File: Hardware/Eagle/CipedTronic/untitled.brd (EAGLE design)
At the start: 100 x 80 mm, 14 parts, among them IC1 ATMEGA48/88/168-PU, T1 BC547

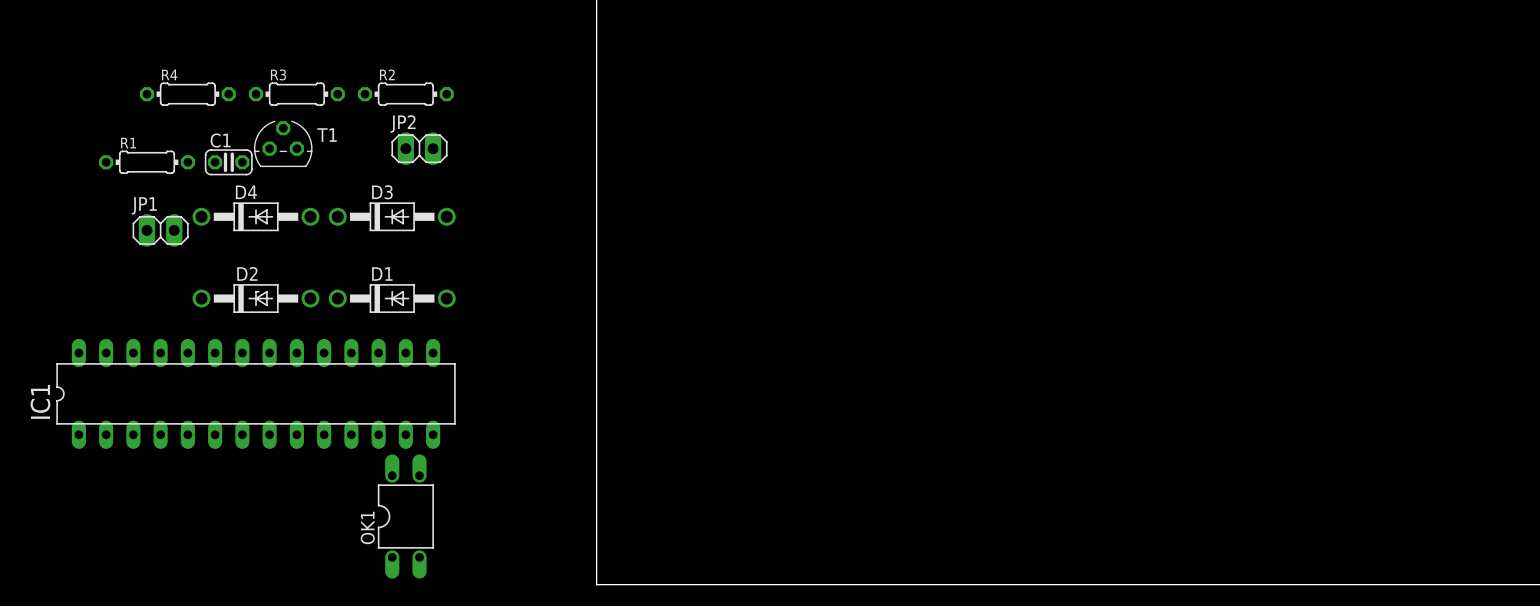
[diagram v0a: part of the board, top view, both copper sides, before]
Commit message: migration to seed xaio esp32
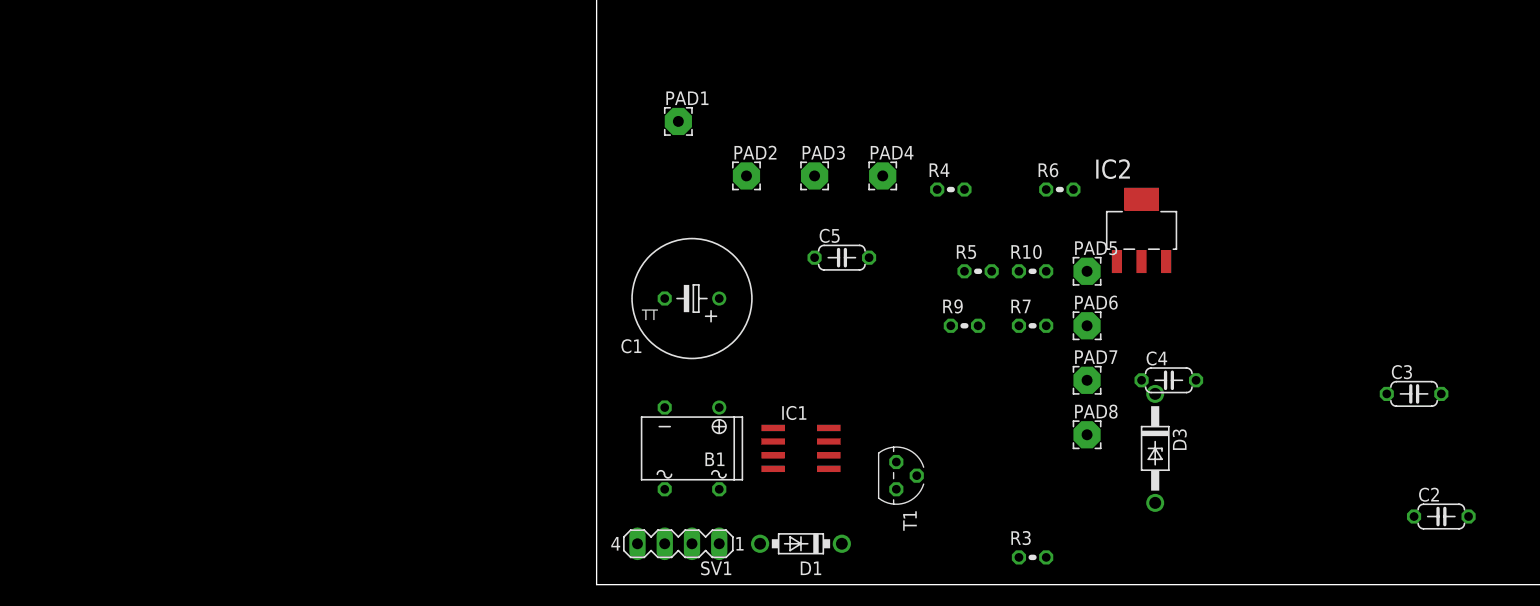
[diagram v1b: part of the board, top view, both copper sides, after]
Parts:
- removed D2: 1N4728, diode:DO41Z10
- removed D4: 1N4004, diode:DO41-10
- removed JP1, JP2: (no value), pinhead:1X02
- removed OK1: SFH610, optocoupler:DIL04
- removed R1, R2: (no value), rcl:0204/7
- added B1: (no value), rectifier:B-DIL
- added C2, C3, C4, C5: (no value), rcl:C050-024X044
- added IC2: LM1117MP-5.0, lm1117_11:SOT223
- added PAD1, PAD2, PAD3, PAD4, PAD5, PAD6, PAD7, PAD8: WIREPAD2,54/1,0, wirepad:2,54/1,0
- added R10, R5, R6, R7, R9: (no value), rcl:0204V
- added SV1: (no value), con-lstb:MA04-1
- C1: device rcl:C025-024X044 -> rcl:TT5D11
- D1: value 1N4004 -> 1N5818-T; device diode:DO41-10 -> diode:DO41-7.6
- D3: value 1N4004 -> 1N4728; device diode:DO41-10 -> diode:DO41Z10
- IC1: value ATMEGA48/88/168-PU -> LM358D; device atmega8:DIL28-3 -> linear:SO08
- R3, R4: device rcl:0204/7 -> rcl:0204V
- T1: value BC547 -> BC337
- moved R3 81.0 mm to (40.6, 2.54)
- moved D3 74.3 mm to (52.1, 12.7), turned to 270 degrees
- moved R4 71.7 mm to (33.0, 36.8)
- moved T1 64.8 mm to (27.9, 10.2), turned to 270 degrees
- moved IC1 51.1 mm to (19.1, 12.7), turned to 270 degrees
- moved C1 45.0 mm to (8.89, 26.7), turned to 180 degrees
- moved D1 44.4 mm to (19.1, 3.81), turned to 180 degrees
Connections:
- removed net N$6: IC1.2, JP1.1
- removed net N$7: OK1.2, T1.3
- new net +3V3: B1.+, C1.+, C4.1, IC1.8, PAD7.1, R3.2, R5.2, R7.2
- new net N$11: IC1.6, R5.1, R6.2
- new net N$12: PAD2.1, PAD3.1
- new net N$4: R9.2, T1.2
- new net V+: IC1.5, PAD1.1, T1.3
- net +5V: now also IC2.2, IC2.4, PAD6.1; no longer C1.1, IC1.20, IC1.7, OK1.3
- net GND: now also B1.-, C1.-, C4.2, C5.1, IC1.2, IC1.4, IC2.1, PAD4.1, PAD8.1, R10.1, R6.1; no longer C1.2, D2.A, D4.C, IC1.22, IC1.8, JP2.1, R3.2, R4.2
- net N$1: now also B1.AC1, C5.2, R4.1, SV1.3, SV1.4; no longer D1.C, R1.2
- net N$10: now also D3.A, R10.2; no longer IC1.3, JP1.2
- net N$2: now also B1.AC2, SV1.1, SV1.2; no longer R3.1, T1.1
- net N$3: now also IC1.1, PAD5.1, R3.1; no longer D3.A, R2.2, T1.2
- net N$5: now also D1.A, D1.C, IC1.3, R4.2; no longer D2.C, OK1.1, R1.1, R2.1
- net N$8: now also IC1.7, R7.1, R9.1; no longer D1.A, JP2.2
- net N$9: now also D3.C, IC2.3, T1.1; no longer IC1.11, OK1.4, R4.1

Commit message: Cipedtronic with esp32
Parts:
- added D2: 1N4728, diode:DO41Z10
- added D4, D5: 1N5818-T, diode:DO41-7.6
- added R1, R8: 10k, rcl:0204V
- added R2: 1m, rcl:0204V
- C2: value (none) -> 0,1uf
- C3: value (none) -> 0.33uf
- R3: value (none) -> 10k
- moved R3 57.7 mm to (3.81, -41.9)
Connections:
- net N$2 renamed V-
- new net N$6: IC1.3, R1.1, R2.2
- new net N$7: D4.A, D4.C, D5.A, IC1.2, R3.2
- net +3V3: now also R3.1, R8.1; no longer R3.2
- net +5V: now also C2.1
- net GND: now also C2.2, C3.2, D2.A, D5.C; no longer IC1.2
- net N$3: now also R2.1, R8.2; no longer R3.1
- net N$5: now also D2.C, R1.2; no longer IC1.3
- net N$9: now also C3.1

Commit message: Rename sketch Extend Timer Add namespace
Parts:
- removed C1: (no value), rcl:TT5D11
- removed D3: 1N4728, diode:DO41Z10
- removed R10, R9: (no value), rcl:0204V
- removed T1: BC337, transistor:TO92
- added PAD10, PAD9: Light on/off switch, wirepad:2,15/1,0
- added Q1, Q3: FDD4141TO252, transistor-fet:TO252
- PAD1: value WIREPAD2,54/1,0 -> Light on/off ESP32; device wirepad:2,54/1,0 -> wirepad:2,15/1,0
- PAD2: value WIREPAD2,54/1,0 -> 5V ESP32; device wirepad:2,54/1,0 -> wirepad:2,15/1,0
- PAD3: value WIREPAD2,54/1,0 -> 3.3V ESP32; device wirepad:2,54/1,0 -> wirepad:2,15/1,0
- PAD4, PAD5: value WIREPAD2,54/1,0 -> LED; device wirepad:2,54/1,0 -> wirepad:2,15/1,0
- PAD6: value WIREPAD2,54/1,0 -> Pulses ESP32; device wirepad:2,54/1,0 -> wirepad:2,15/1,0
- PAD7, PAD8: value WIREPAD2,54/1,0 -> Super Cap; device wirepad:2,54/1,0 -> wirepad:2,15/1,0
- R5: value (none) -> 10k; device rcl:0204V -> rcl:MINI_MELF-0204W
- R6, R7: value (none) -> 10k
- moved R8 72.4 mm to (6.35, 24.1)
- moved R2 69.3 mm to (36.8, 40.6)
- moved D4 65.9 mm to (22.9, 36.8)
- moved D5 64.3 mm to (15.2, 29.2)
- moved R3 63.1 mm to (14.0, 20.3)
- moved R1 51.6 mm to (12.7, 35.6)
- moved C3 49.5 mm to (26.7, 19.1)
- moved PAD6 44.9 mm to (1.27, 17.8)
- moved PAD7 44.9 mm to (1.27, 12.7)
- moved PAD8 44.9 mm to (1.27, 7.62)
- moved R7 44.3 mm to (1.27, 44.5)
- moved C2 37.5 mm to (45.7, 24.1), turned to 90 degrees
- moved D2 36.1 mm to (17.8, 25.4)
- moved C4 26.9 mm to (26.7, 15.2)
- moved PAD3 21.6 mm to (1.27, 27.9)
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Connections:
- removed net N$10: D3.A, R10.2
- removed net N$11: IC1.6, R5.1, R6.2
- removed net N$12: PAD2.1, PAD3.1
- new net N$13: D1.A, R4.2
- new net N$2: PAD4.1, Q3.3
- net +3V3: now also PAD10.1, PAD2.1; no longer C1.+, R5.2, R7.2
- net +5V: now also PAD3.1; no longer PAD6.1
- net GND: now also PAD5.1, R5.2, R7.2; no longer C1.-, PAD4.1, R10.1, R6.1
- net N$3: now also PAD6.1; no longer PAD5.1
- net N$4: now also C3.1, IC2.3, Q1.3; no longer R9.2, T1.2
- net N$5: no longer D1.A, R4.2
- net N$8: now also PAD1.1, PAD9.1, Q3.1; no longer IC1.7, R9.1
- net N$9: now also Q1.1, R5.1, R6.2; no longer C3.1, D3.C, IC2.3, T1.1
- net V+: now also Q1.2, Q3.2, R6.1; no longer IC1.5, PAD1.1, T1.3
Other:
- board size 100 x 80 mm -> 50 x 50 mm

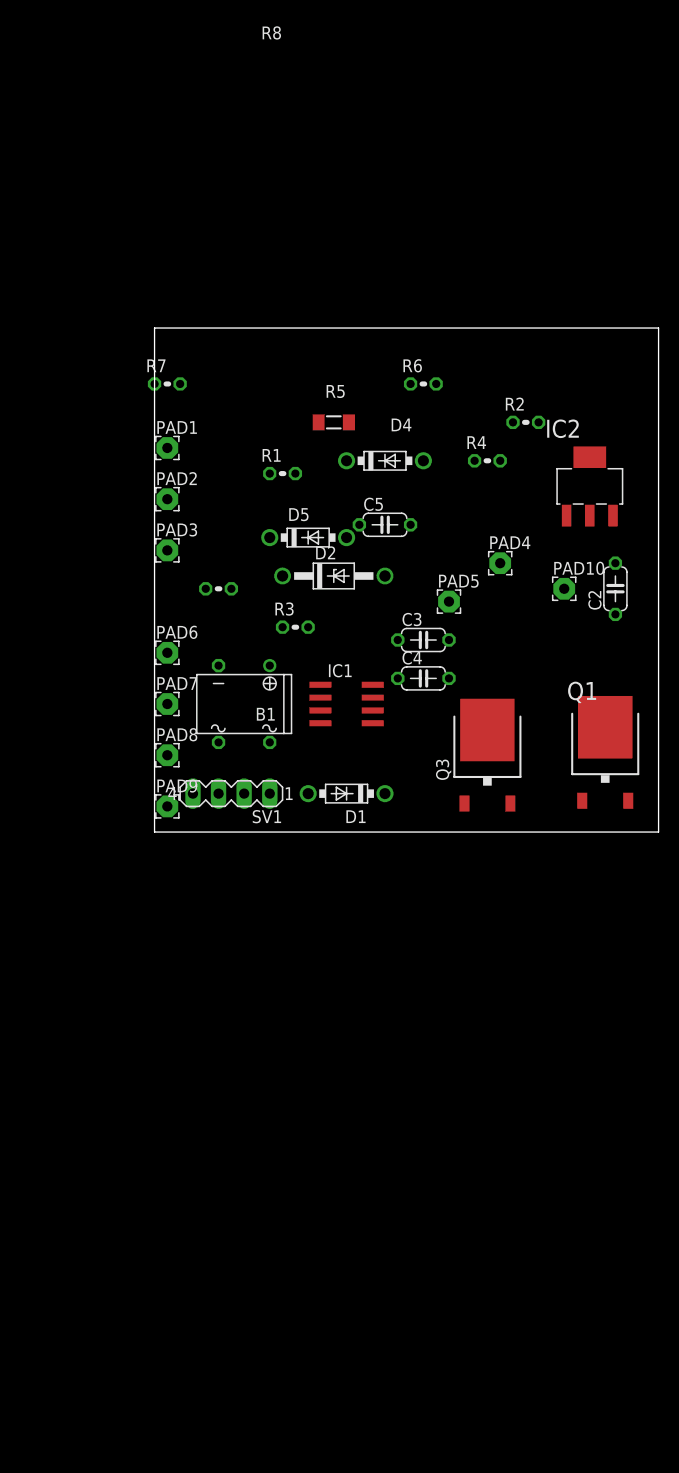
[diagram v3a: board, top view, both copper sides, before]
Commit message: battery load functions distance sensor improved pulse formatting
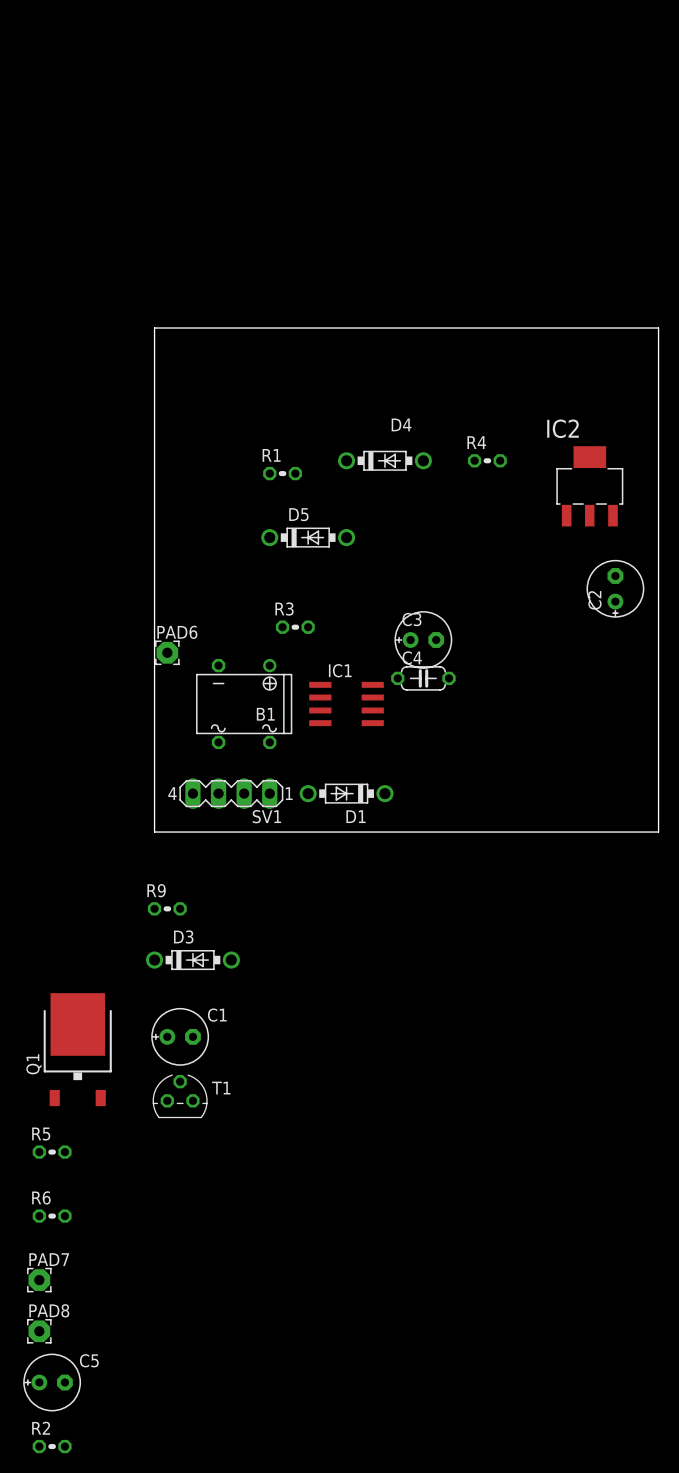
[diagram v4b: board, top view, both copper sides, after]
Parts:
- removed D2: 1N4728, diode:DO41Z10
- removed PAD1: Light on/off ESP32, wirepad:2,15/1,0
- removed PAD10, PAD9: Light on/off switch, wirepad:2,15/1,0
- removed PAD2: 5V ESP32, wirepad:2,15/1,0
- removed PAD3: 3.3V ESP32, wirepad:2,15/1,0
- removed PAD4, PAD5: LED, wirepad:2,15/1,0
- removed Q3: FDD4141TO252, transistor-fet:TO252
- removed R7, R8: 10k, rcl:0204V
- added C1: 5F, rcl:E2,5-6E
- added D3: 1N5818-T, diode:DO41-7.6
- added R9: 33K, rcl:0204V
- added T1: BC547, transistor:TO92
- C2: value 0,1uf -> 10uF; device rcl:C050-024X044 -> rcl:E2,5-6E
- C3: value 0.33uf -> 10uF; device rcl:C050-024X044 -> rcl:E2,5-6E
- C5: value (none) -> 470uF; device rcl:C050-024X044 -> rcl:E2,5-6E
- PAD7: value Super Cap -> LOADENABLE ESP32
- PAD8: value Super Cap -> 5V ESP32
- R2: value 1m -> 1M
- R4: value (none) -> 33K
- R5: device rcl:MINI_MELF-0204W -> rcl:0204V
- moved R2 111.9 mm to (-10.2, -61.0)
- moved C5 91.3 mm to (-10.2, -54.6)
- moved R6 90.4 mm to (-10.2, -38.1)
- moved R5 77.6 mm to (-10.2, -31.8)
- moved Q1 60.1 mm to (-7.62, -21.6)
- moved PAD7 58.5 mm to (-11.4, -44.5)
- moved PAD8 58.5 mm to (-11.4, -49.5)
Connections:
- removed net N$1: B1.AC1, C5.2, R4.1, SV1.3, SV1.4
- removed net N$13: D1.A, R4.2
- removed net N$2: PAD4.1, Q3.3
- removed net N$8: PAD1.1, PAD9.1, Q3.1, R7.1
- removed net V-: B1.AC2, SV1.1, SV1.2
- new net 0V: B1.AC2, R9.1, SV1.1, SV1.2
- new net N$10: PAD8.1, Q1.3
- new net N$11: D1.C, D3.A, R1.2, R4.2
- new net VPP: B1.AC1, R4.1, SV1.3, SV1.4
- net +3V3: now also C1.+, D3.C; no longer PAD10.1, PAD2.1, PAD7.1, R8.1
- net +5V: now also C2.+, C5.+, Q1.2, R5.1; no longer C2.1, PAD3.1
- net GND: now also C1.-, C2.-, C3.-, C5.-, D1.A, R9.2, T1.1; no longer C2.2, C3.2, C5.1, D2.A, PAD5.1, PAD8.1, R5.2, R7.2
- net N$3: now also R2.2; no longer R2.1, R8.2
- net N$4: now also PAD7.1, R6.1; no longer C3.1, IC2.3, Q1.3
- net N$5: now also R6.2, T1.2; no longer D1.C, D2.C, R1.2
- net N$6: now also R2.1; no longer R2.2
- net N$9: now also R5.2, T1.3; no longer R5.1, R6.2
- net V+: now also C3.+, IC2.3; no longer Q1.2, Q3.2, R6.1
